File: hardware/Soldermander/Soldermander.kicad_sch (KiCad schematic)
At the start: 0 parts

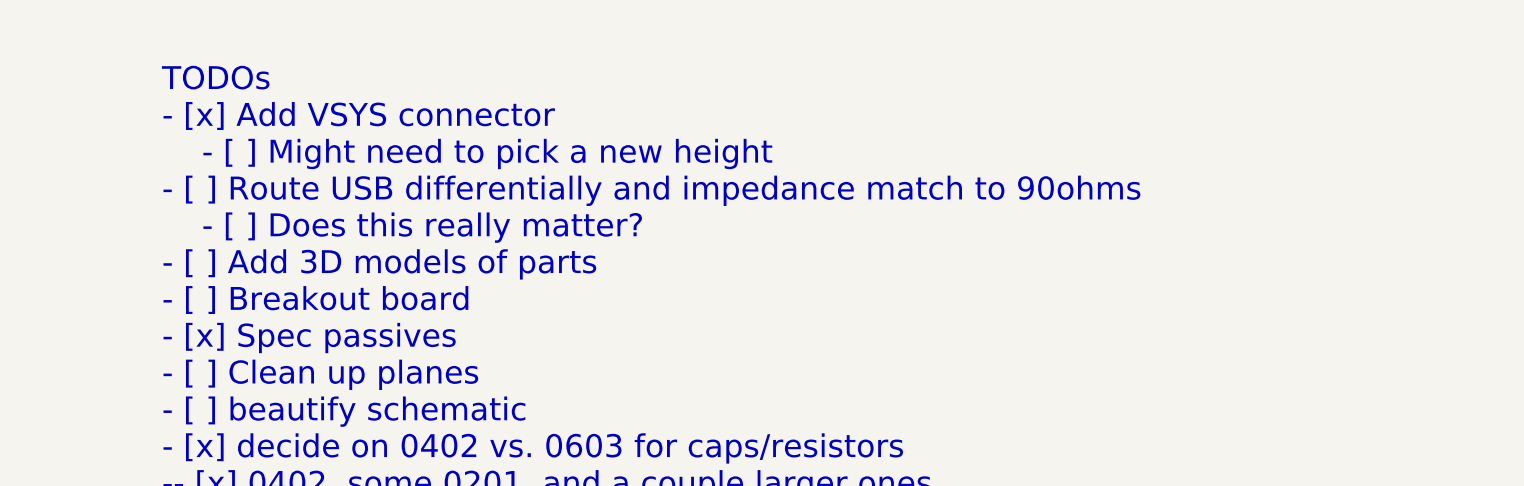
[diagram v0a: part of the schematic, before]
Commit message: update 3.3uH inductor
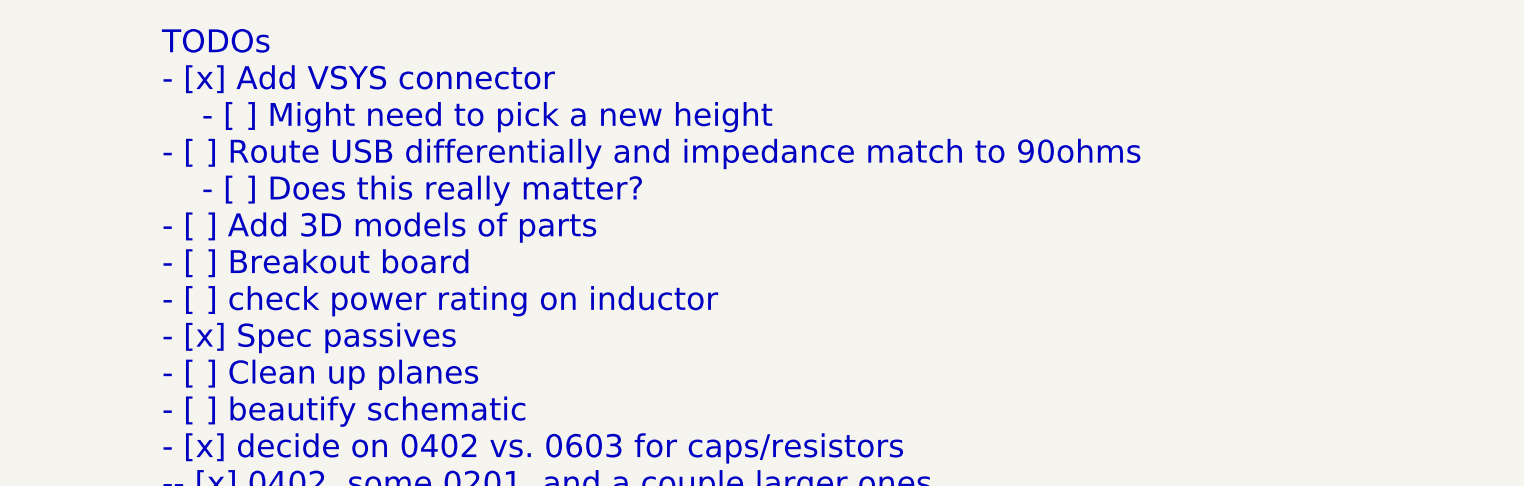
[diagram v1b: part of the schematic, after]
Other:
- note added: "TODOs - [x] Add VSYS connector - [ ] Might need to pick a new height - [ ] Route USB differentially and impedance match to 90ohms - [ ] Does this really matter? - [ ] Add 3D models of parts - [ ] Breakout board - [ ] check power rating on inductor - [x] Spec passives - [ ] Clean up planes - [ ] beautify schematic - [x] decide on 0402 vs. 0603 for caps/resistors -- [x] 0402, some 0201, and a coupl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"
- note removed: "TODOs - [x] Add VSYS connector - [ ] Might need to pick a new height - [ ] Route USB differentially and impedance match to 90ohms - [ ] Does this really matter? - [ ] Add 3D models of parts - [ ] Breakout board - [x] Spec passives - [ ] Clean up planes - [ ] beautify schematic - [x] decide on 0402 vs. 0603 for caps/resistors -- [x] 0402, some 0201, and a couple larger ones -- [x] make the RT1176 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"
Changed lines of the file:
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@@
     (effects (font (size 2.54 2.54) (color 132 0 0 1)) (justify left bottom))
   )
-  (text "TODOs\n- [x] Add VSYS connector\n    - [ ] Might need to pick a new height\n- [ ] Route USB differentially and impedance match to 90ohms\n    - [ ] Does this really matter?\n- [ ] Add 3D models of parts\n- [ ] Breakout board\n- [x] Spec passives\n- [ ] Clean up planes\n- [ ] beautify schematic\n- [x] decide on 0402 vs. 0603 for caps/resistors\n-- [x] 0402, some 0201, and a couple larger ones\n-- [x] make the RT1176 boxes wider\n- [x] Switch fixed regs to variable\n- [x] Make sure most components are on JLCPCB\n- [x] Double check GPIOs and GPIO voltages\n- [x] Fix the $source_resistor\n- [x] Double check D1/D2\n- [x] add boot config switches\n- [x] add boot circuitry\n- [x] double check xSPI MRAM\n- [x] clean up label sizing\n- [x] Finish putting caps on\n- [x] Route MRAM & Flash\n    - [x] Clean up MRAM and flash\n- [x] Route \n- [x] Try patching up ground\n- [x] Pick hole locations\n- [x] Pick a UART for inter-board communications\n- [x] Add JLC P/Ns\n- [x] Double check passive specifications\n- [x] Double check paste layer (or just replace footprints)\n- [x] Put part outlines for things I copied from the coral\n- [x] Route GPIO breakouts\n- [x] Tune SDRAM trace lengths (within 10mm)\n- [x] Tune Crystal trace lengths (within 0.02mm)\n- [x] Add power pins (Low priority)\n- [x] Clean up silkscreen\n"
+  (text "TODOs\n- [x] Add VSYS connector\n    - [ ] Might need to pick a new height\n- [ ] Route USB differentially and impedance match to 90ohms\n    - [ ] Does this really matter?\n- [ ] Add 3D models of parts\n- [ ] Breakout board\n- [ ] check power rating on inductor\n- [x] Spec passives\n- [ ] Clean up planes\n- [ ] beautify schematic\n- [x] decide on 0402 vs. 0603 for caps/resistors\n-- [x] 0402, some 0201, and a couple larger ones\n-- [x] make the RT1176 boxes wider\n- [x] Switch fixed regs to variable\n- [x] Make sure most components are on JLCPCB\n- [x] Double check GPIOs and GPIO voltages\n- [x] Fix the $source_resistor\n- [x] Double check D1/D2\n- [x] add boot config switches\n- [x] add boot circuitry\n- [x] double check xSPI MRAM\n- [x] clean up label sizing\n- [x] Finish putting caps on\n- [x] Route MRAM & Flash\n    - [x] Clean up MRAM and flash\n- [x] Route \n- [x] Try patching up ground\n- [x] Pick hole locations\n- [x] Pick a UART for inter-board communications\n- [x] Add JLC P/Ns\n- [x] Double check passive specifications\n- [x] Double check paste layer (or just replace footprints)\n- [x] Put part outlines for things I copied from the coral\n- [x] Route GPIO breakouts\n- [x] Tune SDRAM trace lengths (within 10mm)\n- [x] Tune Crystal trace lengths (within 0.02mm)\n- [x] Add power pins (Low priority)\n- [x] Clean up silkscreen\n"
     (at 306.705 168.275 0)
     (effects (font (size 2.54 2.54)) (justify left bottom))
@@
     )
     (instances
-      (project "cpu_board"
+      (project "Soldermander"
         (path "/c4fd7bdd-408e-44be-b66f-e6a18a0ca6e3" (page "4"))
       )
@@
     )
     (instances
-      (project "cpu_board"
+      (project "Soldermander"
         (path "/c4fd7bdd-408e-44be-b66f-e6a18a0ca6e3" (page "3"))
       )
@@
     )
     (instances
-      (project "cpu_board"
+      (project "Soldermander"
         (path "/c4fd7bdd-408e-44be-b66f-e6a18a0ca6e3" (page "7"))
       )
@@
     )
     (instances
-      (project "cpu_board"
+      (project "Soldermander"
         (path "/c4fd7bdd-408e-44be-b66f-e6a18a0ca6e3" (page "8"))
       )
@@
     )
     (instances
-      (project "cpu_board"
+      (project "Soldermander"
         (path "/c4fd7bdd-408e-44be-b66f-e6a18a0ca6e3" (page "12"))
       )
@@
     )
     (instances
-      (project "cpu_board"
+      (project "Soldermander"
         (path "/c4fd7bdd-408e-44be-b66f-e6a18a0ca6e3" (page "5"))
       )
@@
     )
     (instances
-      (project "cpu_board"
+      (project "Soldermander"
         (path "/c4fd7bdd-408e-44be-b66f-e6a18a0ca6e3" (page "2"))
       )
@@
     )
     (instances
-      (project "cpu_board"
+      (project "Soldermander"
         (path "/c4fd7bdd-408e-44be-b66f-e6a18a0ca6e3" (page "9"))
       )
@@
     )
     (instances
-      (project "cpu_board"
+      (project "Soldermander"
         (path "/c4fd7bdd-408e-44be-b66f-e6a18a0ca6e3" (page "6"))
       )
@@
     )
     (instances
-      (project "cpu_board"
+      (project "Soldermander"
         (path "/c4fd7bdd-408e-44be-b66f-e6a18a0ca6e3" (page "11"))
       )
